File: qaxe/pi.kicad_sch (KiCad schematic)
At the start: 43 parts, among them J4 Conn_01x02, J5 Conn_01x02, J5 SWD, J6 USB_C_Receptacle_USB2.0, M2 Fan_4pin, U13 TMP1075, U35 STM32L151C8TxA, U37 TXU0101, U39 TXU0101, X1 8MHz

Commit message: updated bom and gerbers
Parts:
- J5: Distributor X -> (none)

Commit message: rev3
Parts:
- added SW1: boot, Button_Switch_SMD:SW_Push_1P1T_NO_CK_KMR2, symbol Switch:SW_Push
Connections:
- net +3V3: now also SW1.2
- net at R23.2, U35.44 (BOOT0): now also SW1.1
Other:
- moved on the sheet: R23
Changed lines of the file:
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@@
   (junction (at 95.885 35.56) (diameter 0) (color 0 0 0 0)
   )
+  (junction (at 70.485 48.26) (diameter 0) (color 0 0 0 0)
+  )
   (junction (at 218.44 48.895) (diameter 0) (color 0 0 0 0)
   )
@@
     (stroke (width 0) (type default))
   )
+  (wire (pts (xy 70.485 48.26) (xy 75.565 48.26))
+    (stroke (width 0) (type default))
+  )
   (wire (pts (xy 90.17 169.545) (xy 88.9 169.545))
     (stroke (width 0) (type default))
@@
     (stroke (width 0) (type default))
   )
+  (wire (pts (xy 70.485 38.1) (xy 70.485 48.26))
+    (stroke (width 0) (type default))
+  )
   (wire (pts (xy 212.09 152.4) (xy 215.9 152.4))
     (stroke (width 0) (type default))
@@
     (stroke (width 0) (type default))
   )
-  (wire (pts (xy 67.31 43.18) (xy 75.565 43.18))
+  (wire (pts (xy 57.15 43.18) (xy 75.565 43.18))
     (stroke (width 0) (type default))
   )
@@
     (stroke (width 0) (type default))
   )
-  (wire (pts (xy 64.135 48.26) (xy 65.405 48.26))
+  (wire (pts (xy 58.42 48.26) (xy 59.69 48.26))
     (stroke (width 0) (type default))
   )
@@
     (stroke (width 0) (type default))
   )
-  (wire (pts (xy 73.025 48.26) (xy 75.565 48.26))
+  (wire (pts (xy 67.31 48.26) (xy 70.485 48.26))
     (stroke (width 0) (type default))
   )
@@
     (stroke (width 0) (type default))
   )
+  (wire (pts (xy 70.485 24.765) (xy 70.485 27.94))
+    (stroke (width 0) (type default))
+  )
   (wire (pts (xy 34.29 22.225) (xy 40.64 22.225))
     (stroke (width 0) (type default))
@@
     (effects (font (size 1.27 1.27)) (justify left bottom))
   )
-  (label "NRST" (at 73.66 43.18 180) (fields_autoplaced)
+  (label "NRST" (at 63.5 43.18 180) (fields_autoplaced)
     (effects (font (size 1.27 1.27)) (justify right bottom))
   )
@@
     )
   )
+  (symbol (lib_id "power:+3V3") (at 70.485 24.765 0) (unit 1)
+    (in_bom yes) (on_board yes) (dnp no) (fields_autoplaced)
+    (property "Reference" "#PWR038" (at 70.485 28.575 0)
+      (effects (font (size 1.27 1.27)) hide)
+    )
+    (property "Value" "+3V3" (at 70.485 19.685 0)
+      (effects (font (size 1.27 1.27)))
+    )
+    (property "Footprint" "" (at 70.485 24.765 0)
+      (effects (font (size 1.27 1.27)) hide)
+    )
+    (property "Datasheet" "" (at 70.485 24.765 0)
+      (effects (font (size 1.27 1.27)) hide)
+    )
+    (pin "1")
+    (instances
+      (project "vfd-night-projector-clock"
+        (path "/58bb089f-6917-42da-8615-90a76037845c"
+          (reference "#PWR038") (unit 1)
+        )
+      )
+      (project "pi"
+        (path "/8e794590-5d75-43f7-90af-cb959cf88b2d"
+          (reference "#PWR020") (unit 1)
+        )
+      )
+      (project "qaxe"
+        (path "/e63e39d7-6ac0-4ffd-8aa3-1841a4541b55/9bc1a7d6-07fa-4858-9423-fb2dbf7da294"
+          (reference "#PWR082") (unit 1)
+        )
+      )
+    )
+  )
   (symbol (lib_name "GND_1") (lib_id "power:GND") (at 190.5 153.67 0) (unit 1)
     (in_bom yes) (on_board yes) (dnp no) (fields_autoplaced)
@@
     )
   )
-  (symbol (lib_id "Device:R") (at 69.215 48.26 90) (unit 1)
+  (symbol (lib_id "Device:R") (at 63.5 48.26 90) (unit 1)
     (in_bom yes) (on_board yes) (dnp no)
-    (property "Reference" "R23" (at 69.215 45.72 90)
+    (property "Reference" "R23" (at 63.5 45.72 90)
       (effects (font (size 1.27 1.27)))
     )
-    (property "Value" "100k" (at 69.215 50.8 90)
+    (property "Value" "100k" (at 63.5 50.8 90)
       (effects (font (size 1.27 1.27)))
     )
-    (property "Footprint" "Resistor_SMD:R_0805_2012Metric" (at 69.215 50.038 90)
+    (property "Footprint" "Resistor_SMD:R_0805_2012Metric" (at 63.5 50.038 90)
       (effects (font (size 1.27 1.27)) hide)
     )
-    (property "Datasheet" "~" (at 69.215 48.26 0)
+    (property "Datasheet" "~" (at 63.5 48.26 0)
       (effects (font (size 1.27 1.27)) hide)
     )
@@
     )
   )
+  (symbol (lib_id "Switch:SW_Push") (at 70.485 33.02 90) (unit 1)
+    (in_bom yes) (on_board yes) (dnp no) (fields_autoplaced)
+    (property "Reference" "SW1" (at 72.39 31.75 90)
+      (effects (font (size 1.27 1.27)) (justify right))
+    )
+    (property "Value" "boot" (at 72.39 34.29 90)
+      (effects (font (size 1.27 1.27)) (justify right))
+    )
+    (property "Footprint" "Button_Switch_SMD:SW_Push_1P1T_NO_CK_KMR2" (at 65.405 33.02 0)
+      (effects (font (size 1.27 1.27)) hide)
+    )
+    (property "Datasheet" "~" (at 65.405 33.02 0)
+      (effects (font (size 1.27 1.27)) hide)
+    )
+    (property "Distributor" "D" (at 70.485 33.02 0)
+      (effects (font (size 1.27 1.27)) hide)
+    )
+    (property "Manufacturer" "KMR221GLFS" (at 70.485 33.02 0)
+      (effects (font (size 1.27 1.27)) hide)
+    )
+    (property "OrderNr" "401-1427-1-ND" (at 70.485 33.02 0)
+      (effects (font (size 1.27 1.27)) hide)
+    )
+    (pin "1")
+    (pin "2")
+    (instances
+      (project "qaxe"
+        (path "/e63e39d7-6ac0-4ffd-8aa3-1841a4541b55/9bc1a7d6-07fa-4858-9423-fb2dbf7da294"
+          (reference "SW1") (unit 1)
+        )
+      )
+    )
+  )
   (symbol (lib_id "clock-rescue:R") (at 52.705 140.97 270) (unit 1)
     (in_bom yes) (on_board yes) (dnp no)
@@
     )
   )
-  (symbol (lib_id "power:GND") (at 64.135 48.26 270) (unit 1)
+  (symbol (lib_id "power:GND") (at 58.42 48.26 270) (unit 1)
     (in_bom yes) (on_board yes) (dnp no) (fields_autoplaced)
-    (property "Reference" "#PWR040" (at 57.785 48.26 0)
+    (property "Reference" "#PWR040" (at 52.07 48.26 0)
       (effects (font (size 1.27 1.27)) hide)
     )
-    (property "Value" "GND" (at 60.325 48.26 90)
+    (property "Value" "GND" (at 54.61 48.26 90)
       (effects (font (size 1.27 1.27)) (justify right))
     )
-    (property "Footprint" "" (at 64.135 48.26 0)
+    (property "Footprint" "" (at 58.42 48.26 0)
       (effects (font (size 1.27 1.27)) hide)
     )
-    (property "Datasheet" "" (at 64.135 48.26 0)
+    (property "Datasheet" "" (at 58.42 48.26 0)
       (effects (font (size 1.27 1.27)) hide)
     )

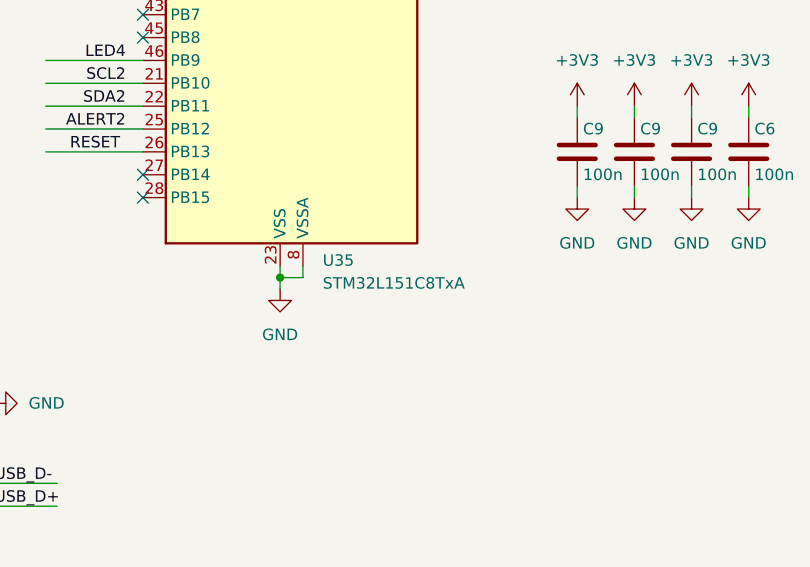
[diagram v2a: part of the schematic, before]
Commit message: bigger stm32 variant that has usb bootloader
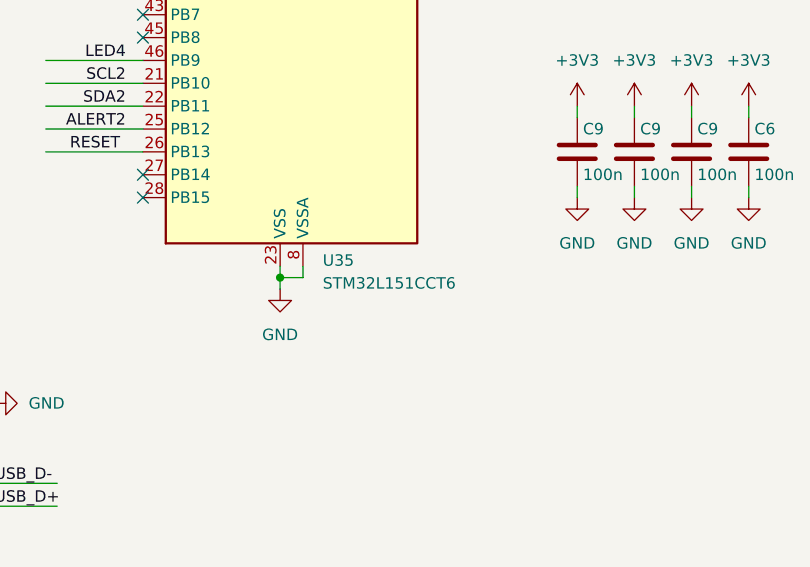
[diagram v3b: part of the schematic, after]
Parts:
- U35: value STM32L151C8TxA -> STM32L151CCT6; Manufacturer STM32L151C8T6A -> STM32L151CCT6; OrderNr 497-17514-ND -> 497-19371-1-ND
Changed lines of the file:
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@@
       (effects (font (size 1.27 1.27)) (justify left))
     )
-    (property "Value" "STM32L151C8TxA" (at 95.5391 118.745 0)
+    (property "Value" "STM32L151CCT6" (at 95.5391 118.745 0)
       (effects (font (size 1.27 1.27)) (justify left))
     )
@@
       (effects (font (size 1.27 1.27)) hide)
     )
-    (property "Manufacturer" "STM32L151C8T6A" (at 90.805 78.74 0)
+    (property "Manufacturer" "STM32L151CCT6" (at 90.805 78.74 0)
       (effects (font (size 1.27 1.27)) hide)
     )
-    (property "OrderNr" "497-17514-ND" (at 90.805 78.74 0)
+    (property "OrderNr" "497-19371-1-ND" (at 90.805 78.74 0)
       (effects (font (size 1.27 1.27)) hide)
     )

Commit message: v0.31
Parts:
- added R26: 10k, Resistor_SMD:R_0805_2012Metric, symbol Device:R
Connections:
- net GND: now also R26.1
- net at U35.20 (PB2): now also R26.2
- no-connect marks 24 -> 23
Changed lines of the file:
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@@
   (no_connect (at 108.585 63.5))
   (no_connect (at 75.565 88.9))
-  (no_connect (at 75.565 76.2))
   (no_connect (at 76.2 177.165))
   (no_connect (at 75.565 83.82))
@@
     (stroke (width 0) (type default))
   )
+  (wire (pts (xy 62.23 76.2) (xy 64.77 76.2))
+    (stroke (width 0) (type default))
+  )
   (wire (pts (xy 147.32 162.56) (xy 147.32 163.83))
     (stroke (width 0) (type default))
@@
     (stroke (width 0) (type default))
   )
+  (wire (pts (xy 72.39 76.2) (xy 75.565 76.2))
+    (stroke (width 0) (type default))
+  )
   (wire (pts (xy 27.305 53.34) (xy 27.305 43.815))
     (stroke (width 0) (type default))
@@
     )
   )
+  (symbol (lib_id "power:GND") (at 62.23 76.2 270) (unit 1)
+    (in_bom yes) (on_board yes) (dnp no) (fields_autoplaced)
+    (property "Reference" "#PWR083" (at 55.88 76.2 0)
+      (effects (font (size 1.27 1.27)) hide)
+    )
+    (property "Value" "GND" (at 58.42 76.2 90)
+      (effects (font (size 1.27 1.27)) (justify right))
+    )
+    (property "Footprint" "" (at 62.23 76.2 0)
+      (effects (font (size 1.27 1.27)) hide)
+    )
+    (property "Datasheet" "" (at 62.23 76.2 0)
+      (effects (font (size 1.27 1.27)) hide)
+    )
+    (pin "1")
+    (instances
+      (project "qaxe"
+        (path "/e63e39d7-6ac0-4ffd-8aa3-1841a4541b55/9bc1a7d6-07fa-4858-9423-fb2dbf7da294"
+          (reference "#PWR083") (unit 1)
+        )
+      )
+    )
+  )
   (symbol (lib_id "power:GND") (at 243.84 153.67 0) (unit 1)
     (in_bom yes) (on_board yes) (dnp no) (fields_autoplaced)
@@
         )
       )
+    )
+  )
+  (symbol (lib_id "Device:R") (at 68.58 76.2 90) (mirror x) (unit 1)
+    (in_bom yes) (on_board yes) (dnp no)
+    (property "Reference" "R26" (at 67.31 78.74 0)
+      (effects (font (size 1.27 1.27)) (justify left))
+    )
+    (property "Value" "10k" (at 69.85 78.74 0)
+      (effects (font (size 1.27 1.27)) (justify left))
+    )
+    (property "Footprint" "Resistor_SMD:R_0805_2012Metric" (at 68.58 74.422 90)
+      (effects (font (size 1.27 1.27)) hide)
+    )
+    (property "Datasheet" "~" (at 68.58 76.2 0)
+      (effects (font (size 1.27 1.27)) hide)
+    )
+    (pin "1")
+    (pin "2")
+    (instances
+      (project "pi"
+        (path "/8e794590-5d75-43f7-90af-cb959cf88b2d"
+          (reference "R26") (unit 1)
+        )
+      )
+      (project "qaxe"
+        (path "/e63e39d7-6ac0-4ffd-8aa3-1841a4541b55/9bc1a7d6-07fa-4858-9423-fb2dbf7da294"
+          (reference "R43") (unit 1)
+        )
+      )

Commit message: 1368 support
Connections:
- net X: now reaches J6.A4 (VBUS), J6.A9 (VBUS), J6.B4 (VBUS), J6.B9 (VBUS)
- no-connect marks 23 -> 22
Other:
- moved on the sheet: C23, C55, C6, C9, D6, J4, J5, J6, M2, R26, R27, R28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
